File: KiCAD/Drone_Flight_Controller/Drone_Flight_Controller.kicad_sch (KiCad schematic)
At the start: 2 parts, among them U1 BNO055, U2 DPS368

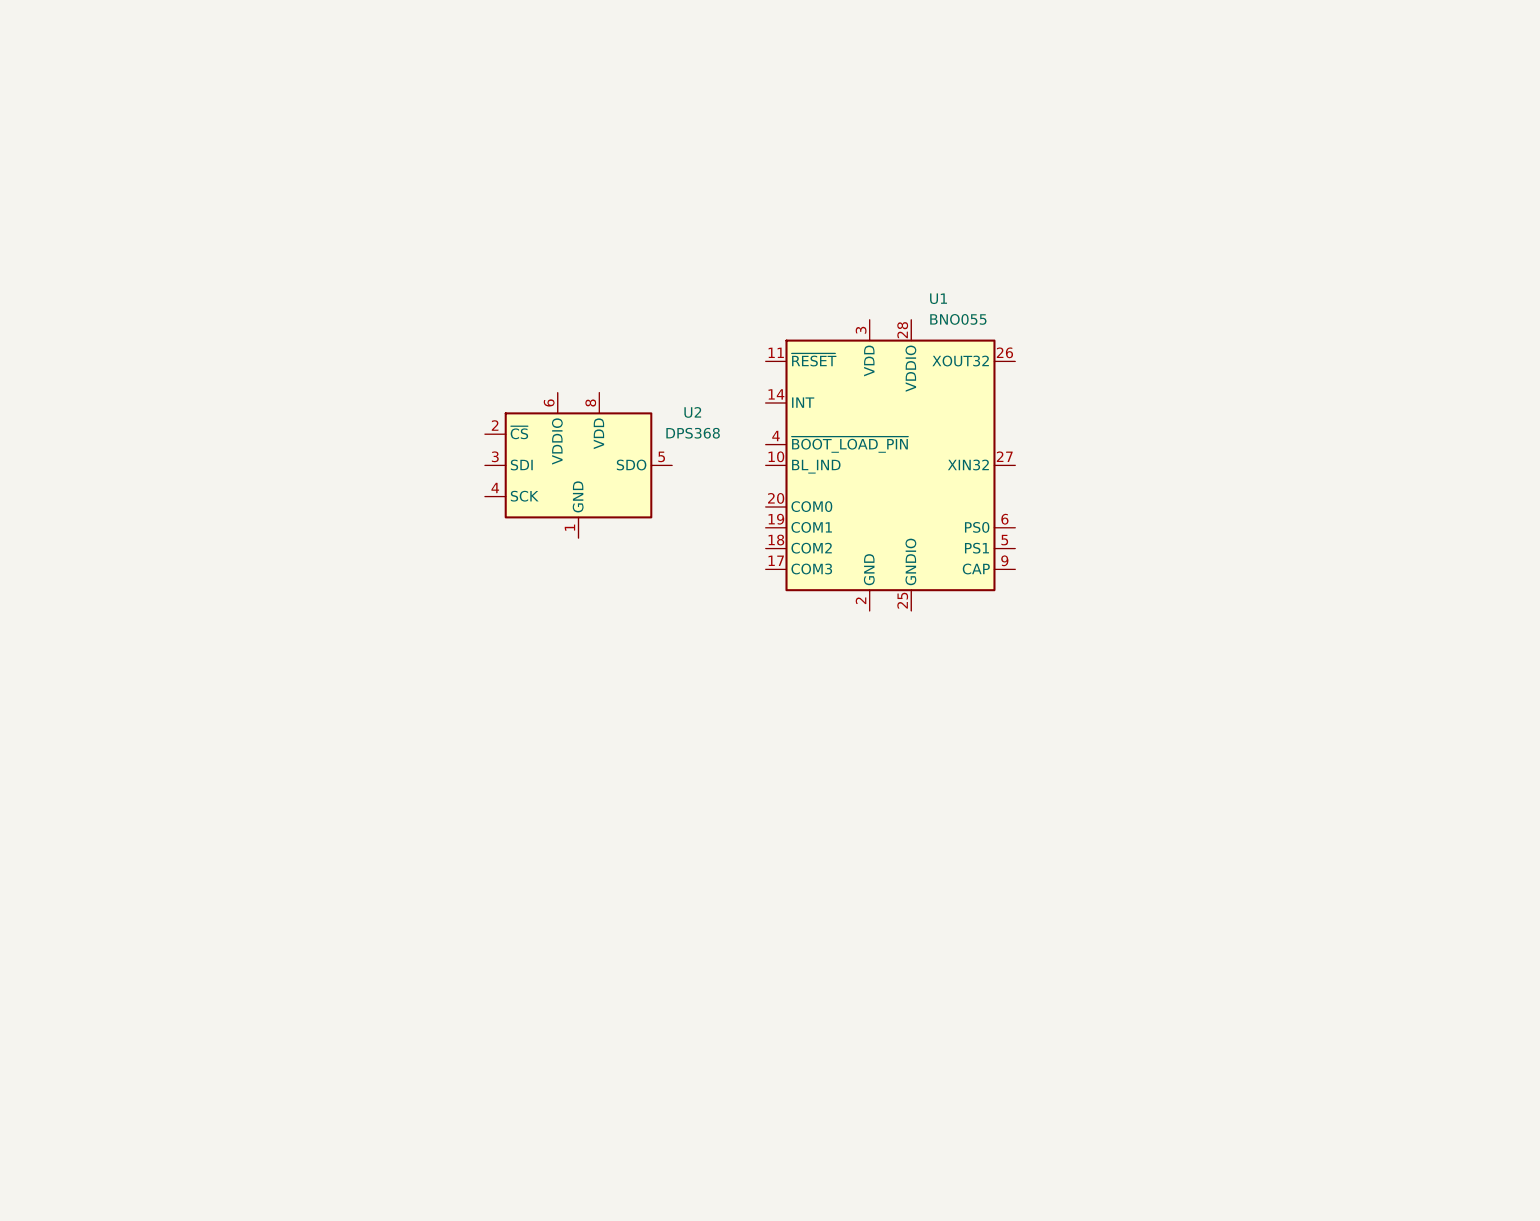
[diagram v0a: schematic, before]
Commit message: Add buzzer and ESP32 symbol. Add Link to components to BOM. Add Names and company to title block.
Add buzzer and ESP32 symbol.
Add Link to components to BOM.
Add Names and company to title block.
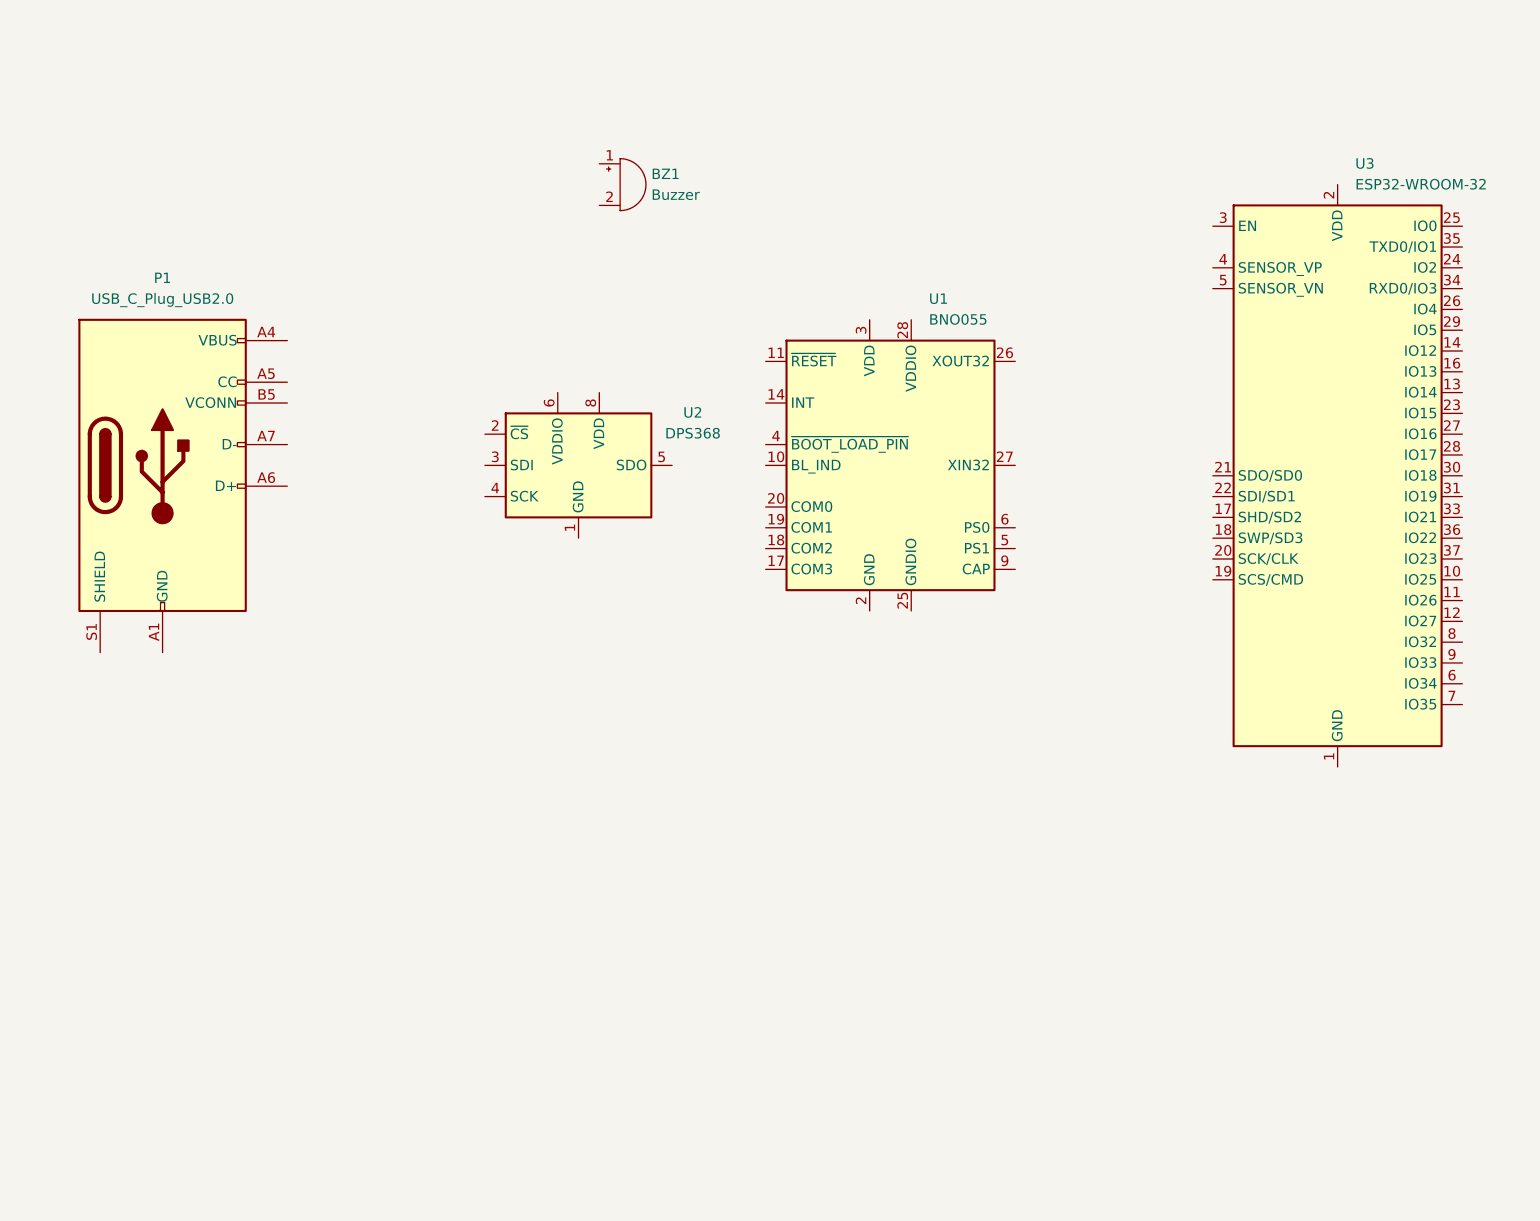
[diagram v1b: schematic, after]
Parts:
- added BZ1: Buzzer, symbol Device:Buzzer
- added P1: USB_C_Plug_USB2.0, symbol Connector:USB_C_Plug_USB2.0
- added U3: ESP32-WROOM-32, RF_Module:ESP32-WROOM-32, symbol RF_Module:ESP32-WROOM-32
- U1: Link (none) -> https://www.mouser.at/ProductDetail/Bosch-Sensortec/BNO055?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
- U2: Link (none) -> https://www.mouser.at/ProductDetail/Infineon-Technologies/D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
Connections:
- new net: U3.1 (GND), U3.15 (GND), U3.38 (GND), U3.39 (GND)
- new net: P1.A1 (GND), P1.A12 (GND), P1.B1 (GND), P1.B12 (GND)
- new net: P1.A4 (VBUS), P1.A9 (VBUS), P1.B4 (VBUS), P1.B9 (VBUS)
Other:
- company: (none) -> HTL Steyr

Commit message: Add Hierarchical Sheets
Add Hierarchical Sheets
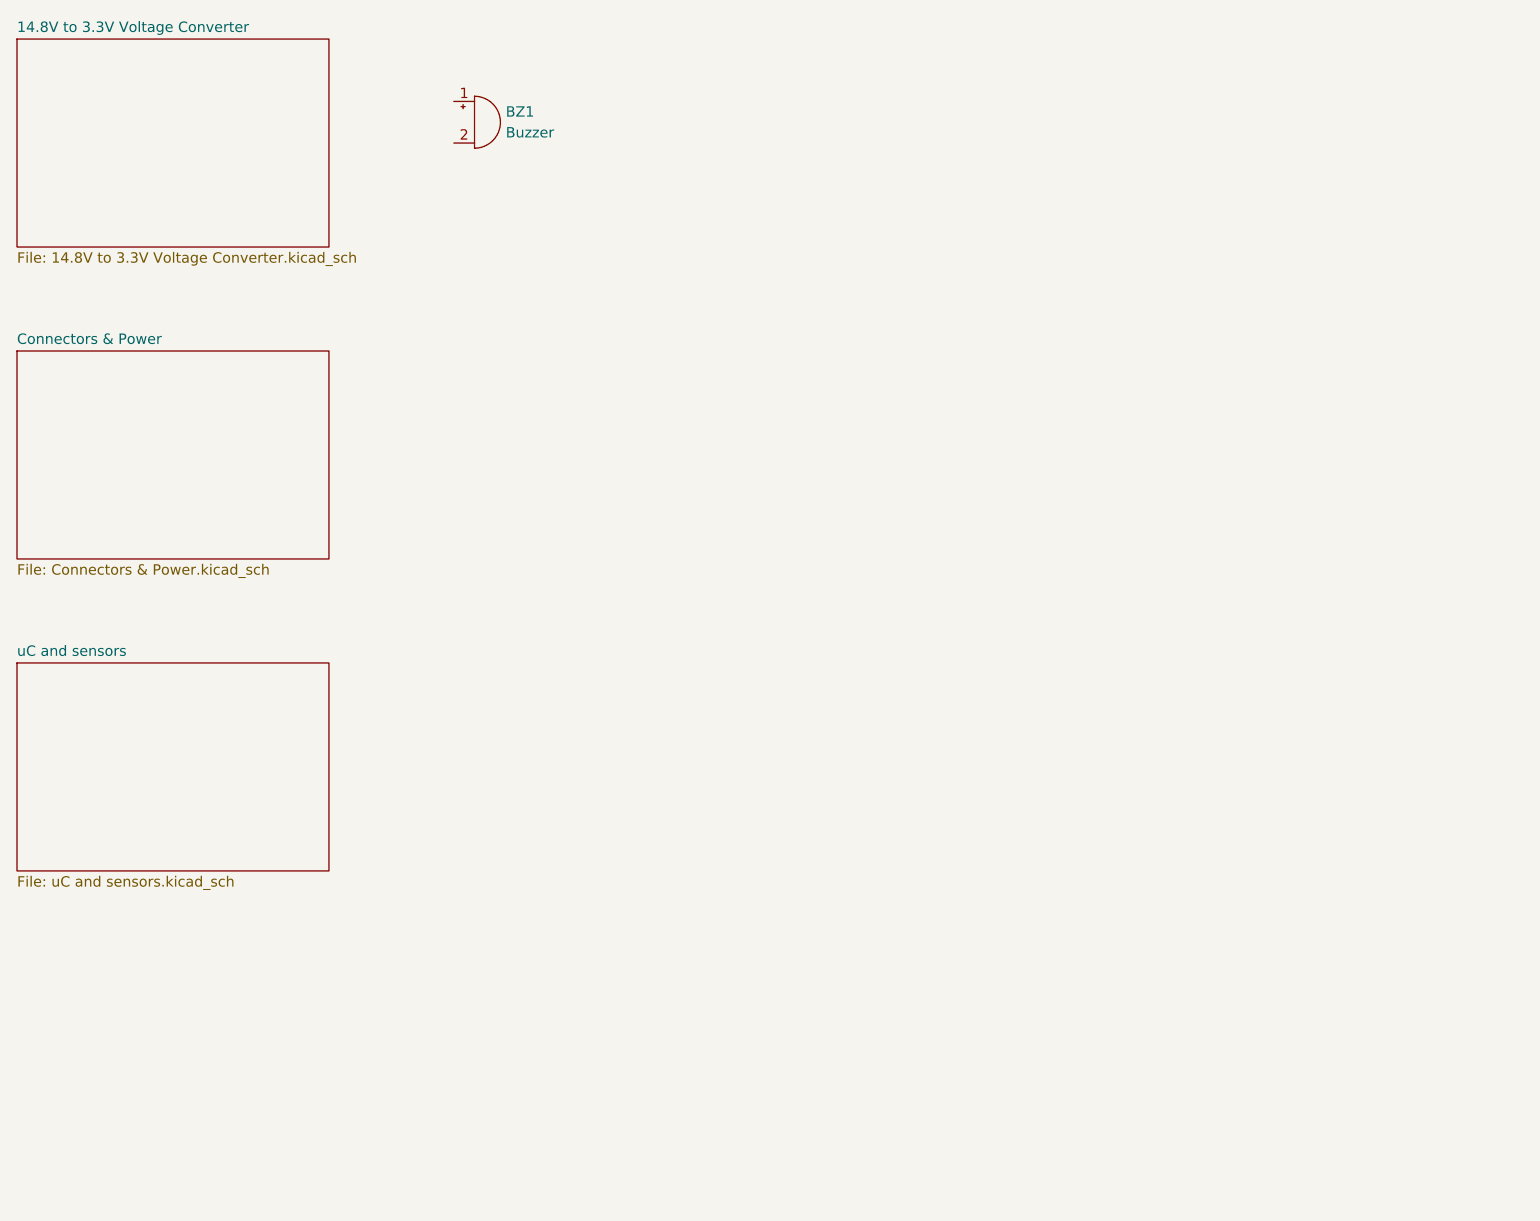
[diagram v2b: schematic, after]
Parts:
- removed P1: USB_C_Plug_USB2.0, symbol Connector:USB_C_Plug_USB2.0
- removed U1: BNO055, Package_LGA:LGA-28_5.2x3.8mm_P0.5mm, symbol Sensor_Motion:BNO055
- removed U2: DPS368, symbol Barometric_Pressure_Sensor:DPS368
- removed U3: ESP32-WROOM-32, RF_Module:ESP32-WROOM-32, symbol RF_Module:ESP32-WROOM-32
- BZ1: footprint (none) -> Buzzer_Beeper:Buzzer_TDK_PS1240P02BT_D12.2mm_H6.5mm; Link https://www.mouser.at/ProductDetail/TDK/PS1240P02CT3?qs=d7g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 -> https://www.mouser.at/ProductDetail/TDK/PS1240P02BT?qs=d7g9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
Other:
- added sheet 14.8V to 3.3V Voltage Converter (14.8V to 3.3V Voltage Converter.kicad_sch)
- added sheet Connectors & Power (Connectors & Power.kicad_sch)
- added sheet uC and sensors (uC and sensors.kicad_sch)
- moved on the sheet: BZ1

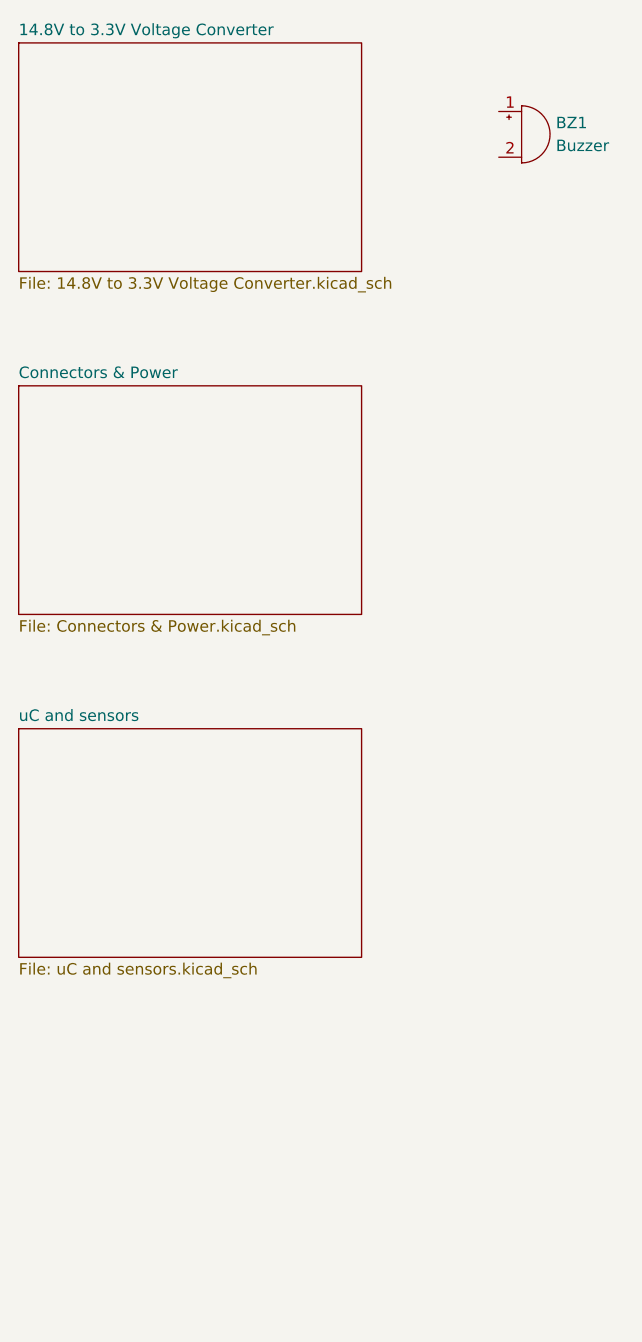
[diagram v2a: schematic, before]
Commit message: Add Buzzer
Add Buzzer
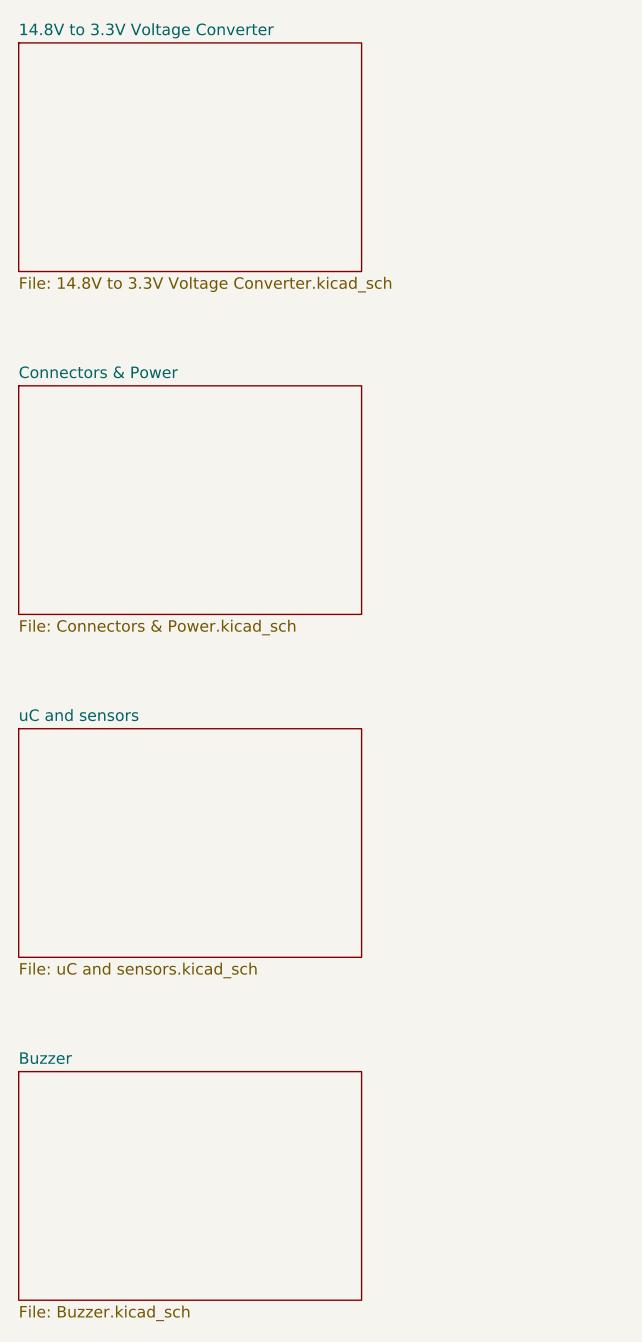
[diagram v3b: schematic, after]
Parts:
- removed BZ1: Buzzer, Buzzer_Beeper:Buzzer_TDK_PS1240P02BT_D12.2mm_H6.5mm, symbol Device:Buzzer
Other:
- added sheet Buzzer (Buzzer.kicad_sch)
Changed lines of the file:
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@@
 		(comment 1 "Brandner; Hinterberger")
-	)
-	(symbol
-		(lib_id "Device:Buzzer")
-		(at 81.28 35.56 0)
-		(unit 1)
-		(exclude_from_sim no)
-		(in_bom yes)
-		(on_board yes)
-		(dnp no)
-		(fields_autoplaced yes)
-		(property "Reference" "BZ1"
-			(at 85.09 34.2899 0)
-			(effects
-				(font
-					(size 1.27 1.27)
-				)
-				(justify left)
-			)
-		)
-		(property "Value" "Buzzer"
-			(at 85.09 36.8299 0)
-			(effects
-				(font
-					(size 1.27 1.27)
-				)
-				(justify left)
-			)
-		)
-		(property "Footprint" "Buzzer_Beeper:Buzzer_TDK_PS1240P02BT_D12.2mm_H6.5mm"
-			(at 80.645 33.02 90)
-			(effects
-				(font
-					(size 1.27 1.27)
-				)
-				(hide yes)
-			)
-		)
-		(property "Datasheet" "https://product.tdk.com/system/files/dam/doc/product/sw_piezo/sw_piezo/piezo-buzzer/catalog/piezoelectronic_buzzer_ps_en.pdf"
-			(at 80.645 33.02 90)
-			(effects
-				(font
-					(size 1.27 1.27)
-				)
-				(hide yes)
-			)
-		)
-		(property "Description" "Buzzer, polarized"
-			(at 81.28 35.56 0)
-			(effects
-				(font
-					(size 1.27 1.27)
-				)
-				(hide yes)
-			)
-		)
-		(property "Link" "https://www.mouser.at/ProductDetail/TDK/PS1240P02BT?qs=d7g9p1yFhWaZXSY9MjKMkw%3D%3D"
-			(at 81.28 35.56 0)
-			(effects
-				(font
-					(size 1.27 1.27)
-				)
-				(hide yes)
-			)
-		)
-		(pin "1"
-		)
-		(pin "2"
-		)
-		(instances
-			(project ""
-				(path "/05daaa24-e506-4b9a-9564-8bf799413ca8"
-					(reference "BZ1")
-					(unit 1)
-				)
-			)
-		)
 	)
 	(sheet
@@
 				)
 			)
+		)
+	)
+	(sheet
+		(at 25.4 139.7)
+		(size 38.1 25.4)
+		(exclude_from_sim no)
+		(in_bom yes)
+		(on_board yes)
+		(dnp no)
+		(fields_autoplaced yes)
+		(stroke
+			(width 0.1524)
+			(type solid)
+		)
+		(fill
+			(color 0 0 0 0.0000)
+		)
+		(property "Sheetname" "Buzzer"
+			(at 25.4 138.9884 0)
+			(effects
+				(font
+					(size 1.27 1.27)
+				)
+				(justify left bottom)
+			)
+		)
+		(property "Sheetfile" "Buzzer.kicad_sch"
+			(at 25.4 165.6846 0)
+			(effects
+				(font
+					(size 1.27 1.27)
+				)
+				(justify left top)
+			)
+		)
+		(instances
+			(project "Drone_Flight_Controller"
+				(path "/05daaa24-e506-4b9a-9564-8bf799413ca8"
+					(page "5")
+				)
+			)

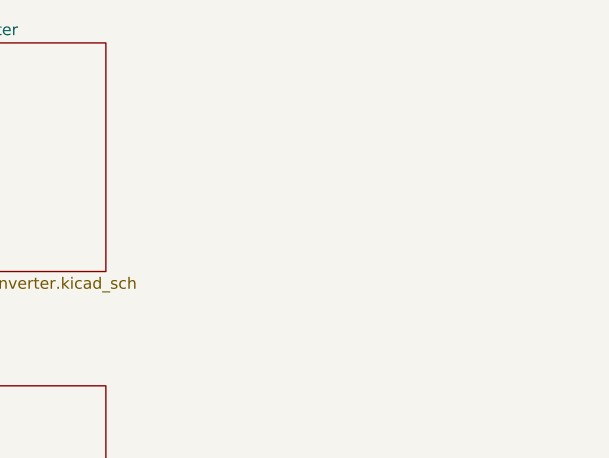
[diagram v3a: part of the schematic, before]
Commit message: Add Battery Monitoring
Add Battery Monitoring
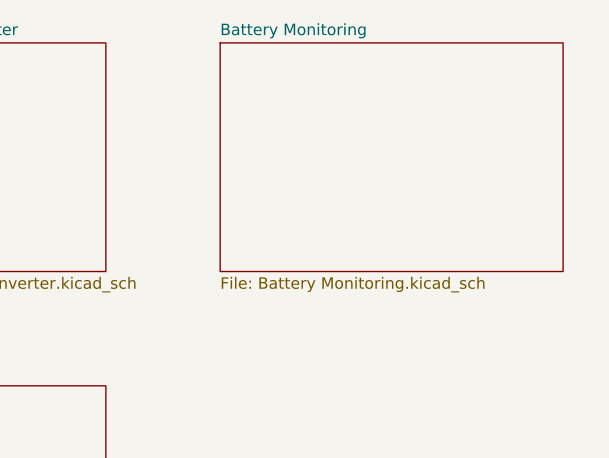
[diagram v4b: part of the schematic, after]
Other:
- added sheet Battery Monitoring (Battery Monitoring.kicad_sch)
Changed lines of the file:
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@@
 	(title_block
 		(title "Drone Flight Controller")
-		(date "2025-06-30")
+		(date "2025-07-07")
 		(rev "V1")
 		(company "HTL Steyr")
@@
 				)
 			)
+		)
+	)
+	(sheet
+		(at 76.2 25.4)
+		(size 38.1 25.4)
+		(exclude_from_sim no)
+		(in_bom yes)
+		(on_board yes)
+		(dnp no)
+		(fields_autoplaced yes)
+		(stroke
+			(width 0.1524)
+			(type solid)
+		)
+		(fill
+			(color 0 0 0 0.0000)
+		)
+		(property "Sheetname" "Battery Monitoring"
+			(at 76.2 24.6884 0)
+			(effects
+				(font
+					(size 1.27 1.27)
+				)
+				(justify left bottom)
+			)
+		)
+		(property "Sheetfile" "Battery Monitoring.kicad_sch"
+			(at 76.2 51.3846 0)
+			(effects
+				(font
+					(size 1.27 1.27)
+				)
+				(justify left top)
+			)
+		)
+		(instances
+			(project "Drone_Flight_Controller"
+				(path "/05daaa24-e506-4b9a-9564-8bf799413ca8"
+					(page "6")
+				)
+			)
